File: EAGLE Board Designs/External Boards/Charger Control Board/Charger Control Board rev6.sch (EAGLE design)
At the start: 112 parts, among them U1 CPC1002N, U2 CDSOT23-T24CAN-Q

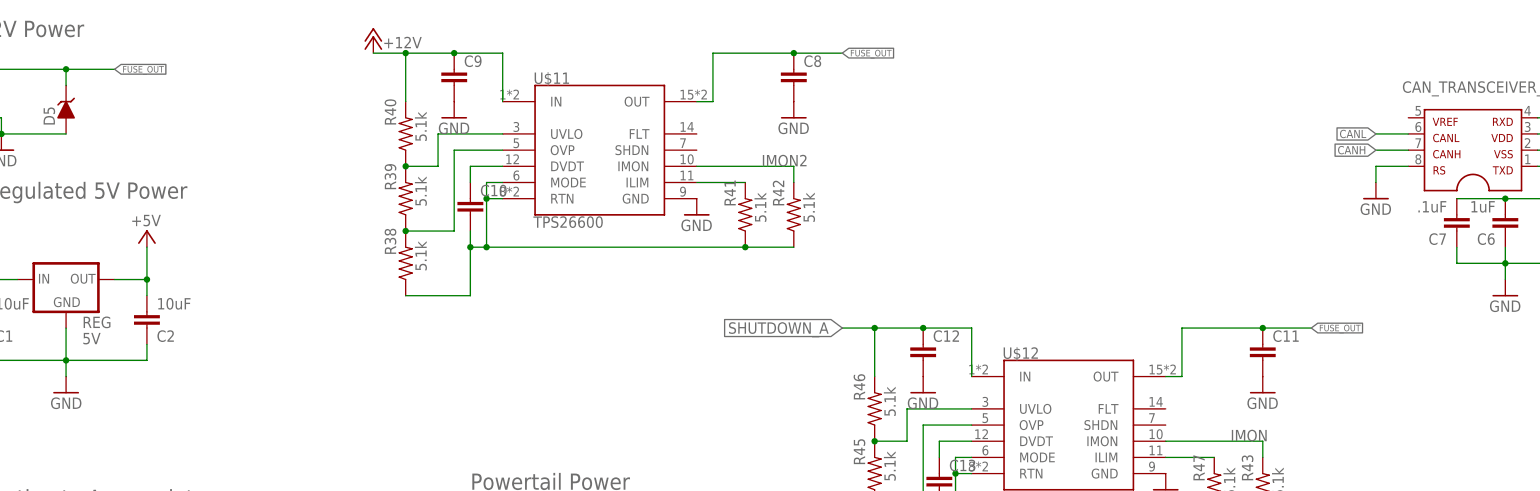
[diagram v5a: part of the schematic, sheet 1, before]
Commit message: Altered the orientation of the e-fuse and made changes to the trace widths
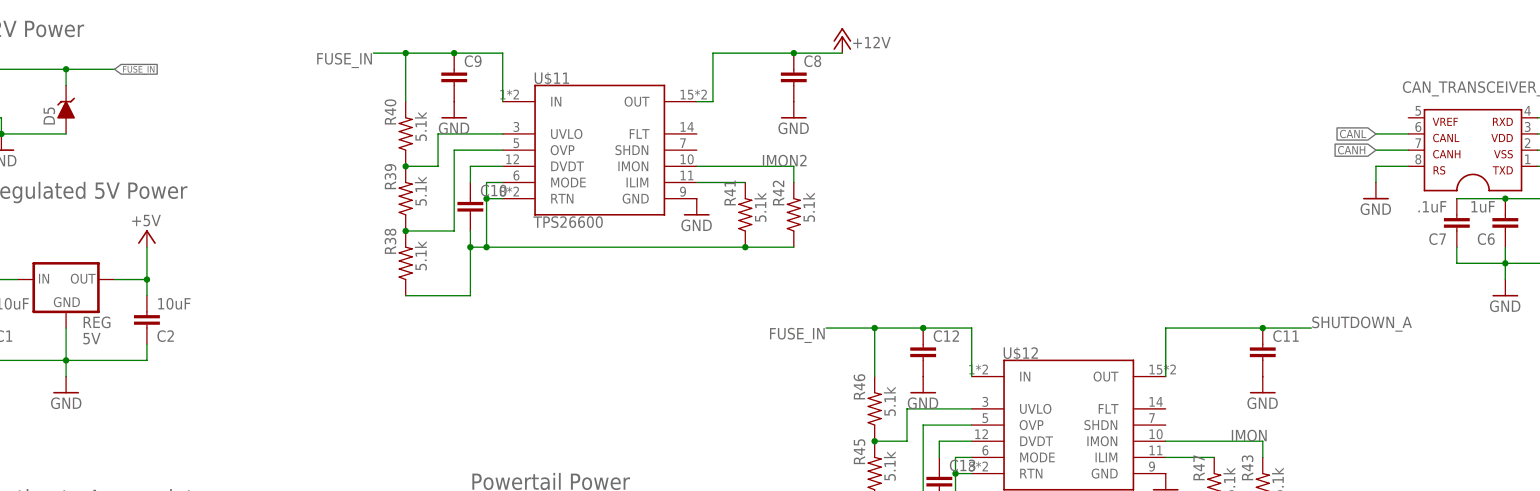
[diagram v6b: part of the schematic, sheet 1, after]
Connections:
- removed net FUSE_OUT: C11.1, C8.1, D5.C, POWER-1.S, POWER-3.S, U$11.OUT, U$12.OUT
- new net FUSE_IN: C12.1, C9.1, D5.C, POWER-1.S, POWER-3.S, R40.2, R46.2, U$11.IN, U$12.IN
- net +12V: now also C8.1, U$11.OUT; no longer C9.1, R40.2, U$11.IN
- net SHUTDOWN_A: now also C11.1, U$12.OUT; no longer C12.1, R46.2, U$12.IN
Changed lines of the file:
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@@
 <part name="R17" library="HyTechDevices" deviceset="RESISTOR" device="0603-RES" value="1k"/>
 <part name="U$7" library="HyTechFrames" deviceset="FRAME_B_L" device=""/>
-<part name="P+5" library="supply1" deviceset="+12V" device=""/>
 <part name="GND2" library="supply1" deviceset="GND" device=""/>
 <part name="REG" library="HyTechDevices" deviceset="OKI-78SR-5" device="" value="5V"/>
@@
 <attribute name="TOLERANCE" value="1%"/>
 </part>
+<part name="P+5" library="supply1" deviceset="+12V" device=""/>
 </parts>
 <sheets>
@@
 <attribute name="DRAWING_NAME" x="356.87" y="22.86" size="2.54" layer="97"/>
 </instance>
-<instance part="P+5" gate="1" x="109.22" y="254" smashed="yes">
-<attribute name="VALUE" x="116.84" y="254" size="1.778" layer="96" rot="R180"/>
-</instance>
 <instance part="GND2" gate="1" x="50.8" y="236.22" smashed="yes">
 <attribute name="VALUE" x="48.26" y="233.68" size="1.778" layer="96"/>
@@
 <attribute name="VALUE" x="252.222" y="181.61" size="1.778" layer="96" rot="R90"/>
 <attribute name="TOLERANCE" x="248.92" y="182.88" size="0.127" layer="96" rot="R90" display="off"/>
+</instance>
+<instance part="P+5" gate="1" x="182.88" y="254" smashed="yes">
+<attribute name="VALUE" x="190.5" y="254" size="1.778" layer="96" rot="R180"/>
 </instance>
 </instances>
@@
 </segment>
 <segment>
-<pinref part="U$11" gate="G$1" pin="IN"/>
-<wire x1="129.54" y1="243.84" x2="129.54" y2="251.46" width="0.1524" layer="91"/>
-<wire x1="129.54" y1="251.46" x2="121.92" y2="251.46" width="0.1524" layer="91"/>
-<pinref part="R40" gate="G$1" pin="2"/>
-<wire x1="121.92" y1="251.46" x2="114.3" y2="251.46" width="0.1524" layer="91"/>
-<wire x1="114.3" y1="251.46" x2="114.3" y2="243.84" width="0.1524" layer="91"/>
-<pinref part="C9" gate="G$1" pin="1"/>
-<junction x="121.92" y="251.46"/>
-<wire x1="114.3" y1="251.46" x2="109.22" y2="251.46" width="0.1524" layer="91"/>
-<junction x="114.3" y="251.46"/>
+<pinref part="U$11" gate="G$1" pin="OUT"/>
+<wire x1="160.02" y1="243.84" x2="162.56" y2="243.84" width="0.1524" layer="91"/>
+<wire x1="162.56" y1="243.84" x2="162.56" y2="251.46" width="0.1524" layer="91"/>
+<wire x1="162.56" y1="251.46" x2="175.26" y2="251.46" width="0.1524" layer="91"/>
+<pinref part="C8" gate="G$1" pin="1"/>
+<wire x1="175.26" y1="251.46" x2="182.88" y2="251.46" width="0.1524" layer="91"/>
+<junction x="175.26" y="251.46"/>
 <pinref part="P+5" gate="1" pin="+12V"/>
 </segment>
@@
 <net name="SHUTDOWN_A" class="0">
 <segment>
-<pinref part="U$12" gate="G$1" pin="IN"/>
-<wire x1="203.2" y1="200.66" x2="203.2" y2="208.28" width="0.1524" layer="91"/>
-<wire x1="203.2" y1="208.28" x2="195.58" y2="208.28" width="0.1524" layer="91"/>
-<pinref part="R46" gate="G$1" pin="2"/>
-<wire x1="195.58" y1="208.28" x2="187.96" y2="208.28" width="0.1524" layer="91"/>
-<wire x1="187.96" y1="208.28" x2="187.96" y2="200.66" width="0.1524" layer="91"/>
-<pinref part="C12" gate="G$1" pin="1"/>
-<junction x="195.58" y="208.28"/>
-<wire x1="187.96" y1="208.28" x2="182.88" y2="208.28" width="0.1524" layer="91"/>
-<junction x="187.96" y="208.28"/>
-<label x="182.88" y="208.28" size="1.778" layer="95" font="vector" rot="R180" xref="yes"/>
-</segment>
-</net>
-<net name="FUSE_OUT" class="0">
+<pinref part="U$12" gate="G$1" pin="OUT"/>
+<pinref part="C11" gate="G$1" pin="1"/>
+<wire x1="233.68" y1="200.66" x2="233.68" y2="208.28" width="0.1524" layer="91"/>
+<wire x1="233.68" y1="208.28" x2="248.92" y2="208.28" width="0.1524" layer="91"/>
+<wire x1="248.92" y1="208.28" x2="256.54" y2="208.28" width="0.1524" layer="91"/>
+<junction x="248.92" y="208.28"/>
+<label x="256.54" y="208.28" size="1.778" layer="95"/>
+</segment>
+</net>
+<net name="IMON" class="0">
+<segment>
+<pinref part="U$12" gate="G$1" pin="IMON"/>
+<label x="243.84" y="190.5" size="1.778" layer="95"/>
+<pinref part="R43" gate="G$1" pin="2"/>
+<wire x1="233.68" y1="190.5" x2="248.92" y2="190.5" width="0.1524" layer="91"/>
+<wire x1="248.92" y1="190.5" x2="248.92" y2="187.96" width="0.1524" layer="91"/>
+</segment>
+<segment>
+<pinref part="U$4" gate="G$1" pin="A6"/>
+<wire x1="121.92" y1="58.42" x2="124.46" y2="58.42" width="0.1524" layer="91"/>
+<label x="124.46" y="58.42" size="1.778" layer="95"/>
+</segment>
+</net>
+<net name="IMON2" class="0">
+<segment>
+<pinref part="U$11" gate="G$1" pin="IMON"/>
+<label x="170.18" y="233.68" size="1.778" layer="95"/>
+<wire x1="160.02" y1="233.68" x2="175.26" y2="233.68" width="0.1524" layer="91"/>
+<pinref part="R42" gate="G$1" pin="2"/>
+<wire x1="175.26" y1="233.68" x2="175.26" y2="231.14" width="0.1524" layer="91"/>
+</segment>
+<segment>
+<pinref part="U$4" gate="G$1" pin="A5"/>
+<wire x1="121.92" y1="55.88" x2="124.46" y2="55.88" width="0.1524" layer="91"/>
+<label x="124.46" y="55.88" size="1.778" layer="95"/>
+</segment>
+</net>
+<net name="FUSE_IN" class="0">
 <segment>
 <wire x1="68.58" y1="248.92" x2="60.96" y2="248.92" width="0.1524" layer="91"/>
@@
 </segment>
 <segment>
-<pinref part="U$11" gate="G$1" pin="OUT"/>
-<wire x1="160.02" y1="243.84" x2="162.56" y2="243.84" width="0.1524" layer="91"/>
-<wire x1="162.56" y1="243.84" x2="162.56" y2="251.46" width="0.1524" layer="91"/>
-<wire x1="162.56" y1="251.46" x2="175.26" y2="251.46" width="0.1524" layer="91"/>
-<pinref part="C8" gate="G$1" pin="1"/>
-<wire x1="175.26" y1="251.46" x2="182.88" y2="251.46" width="0.1524" layer="91"/>
-<junction x="175.26" y="251.46"/>
-<label x="182.88" y="251.46" size="1.016" layer="95" font="vector" xref="yes"/>
-</segment>
-<segment>
-<pinref part="U$12" gate="G$1" pin="OUT"/>
-<wire x1="233.68" y1="200.66" x2="236.22" y2="200.66" width="0.1524" layer="91"/>
-<wire x1="236.22" y1="200.66" x2="236.22" y2="208.28" width="0.1524" layer="91"/>
-<wire x1="236.22" y1="208.28" x2="248.92" y2="208.28" width="0.1524" layer="91"/>
-<pinref part="C11" gate="G$1" pin="1"/>
-<wire x1="248.92" y1="208.28" x2="256.54" y2="208.28" width="0.1524" layer="91"/>
-<junction x="248.92" y="208.28"/>
-<label x="256.54" y="208.28" size="1.016" layer="95" font="vector" xref="yes"/>
-</segment>
-</net>
-<net name="IMON" class="0">
-<segment>
-<pinref part="U$12" gate="G$1" pin="IMON"/>
-<label x="243.84" y="190.5" size="1.778" layer="95"/>
-<pinref part="R43" gate="G$1" pin="2"/>
-<wire x1="233.68" y1="190.5" x2="248.92" y2="190.5" width="0.1524" layer="91"/>
-<wire x1="248.92" y1="190.5" x2="248.92" y2="187.96" width="0.1524" layer="91"/>
-</segment>
-<segment>
-<pinref part="U$4" gate="G$1" pin="A6"/>
-<wire x1="121.92" y1="58.42" x2="124.46" y2="58.42" width="0.1524" layer="91"/>
-<label x="124.46" y="58.42" size="1.778" layer="95"/>
-</segment>
-</net>
-<net name="IMON2" class="0">
-<segment>
-<pinref part="U$11" gate="G$1" pin="IMON"/>
-<label x="170.18" y="233.68" size="1.778" layer="95"/>
-<wire x1="160.02" y1="233.68" x2="175.26" y2="233.68" width="0.1524" layer="91"/>
-<pinref part="R42" gate="G$1" pin="2"/>
-<wire x1="175.26" y1="233.68" x2="175.26" y2="231.14" width="0.1524" layer="91"/>
-</segment>
-<segment>
-<pinref part="U$4" gate="G$1" pin="A5"/>
-<wire x1="121.92" y1="55.88" x2="124.46" y2="55.88" width="0.1524" layer="91"/>
-<label x="124.46" y="55.88" size="1.778" layer="95"/>
-</segment>
-</net>
+<pinref part="U$11" gate="G$1" pin="IN"/>
+<wire x1="129.54" y1="243.84" x2="129.54" y2="251.46" width="0.1524" layer="91"/>
+<wire x1="129.54" y1="251.46" x2="121.92" y2="251.46" width="0.1524" layer="91"/>
+<pinref part="R40" gate="G$1" pin="2"/>
+<wire x1="121.92" y1="251.46" x2="114.3" y2="251.46" width="0.1524" layer="91"/>
+<wire x1="114.3" y1="251.46" x2="114.3" y2="243.84" width="0.1524" layer="91"/>
+<pinref part="C9" gate="G$1" pin="1"/>
+<junction x="121.92" y="251.46"/>
+<wire x1="114.3" y1="251.46" x2="109.22" y2="251.46" width="0.1524" layer="91"/>
+<junction x="114.3" y="251.46"/>
+<label x="109.22" y="251.46" size="1.778" layer="95" rot="R180"/>
+</segment>
+<segment>
+<pinref part="U$12" gate="G$1" pin="IN"/>
+<pinref part="C12" gate="G$1" pin="1"/>
+<wire x1="203.2" y1="200.66" x2="203.2" y2="208.28" width="0.1524" layer="91"/>
+<wire x1="203.2" y1="208.28" x2="195.58" y2="208.28" width="0.1524" layer="91"/>
+<pinref part="R46" gate="G$1" pin="2"/>
+<wire x1="195.58" y1="208.28" x2="187.96" y2="208.28" width="0.1524" layer="91"/>
+<wire x1="187.96" y1="208.28" x2="187.96" y2="200.66" width="0.1524" layer="91"/>
+<junction x="195.58" y="208.28"/>
+<wire x1="187.96" y1="208.28" x2="180.34" y2="208.28" width="0.1524" layer="91"/>
+<junction x="187.96" y="208.28"/>
+<label x="180.34" y="208.28" size="1.778" layer="95" rot="R180"/>
+</segment>
+</net>

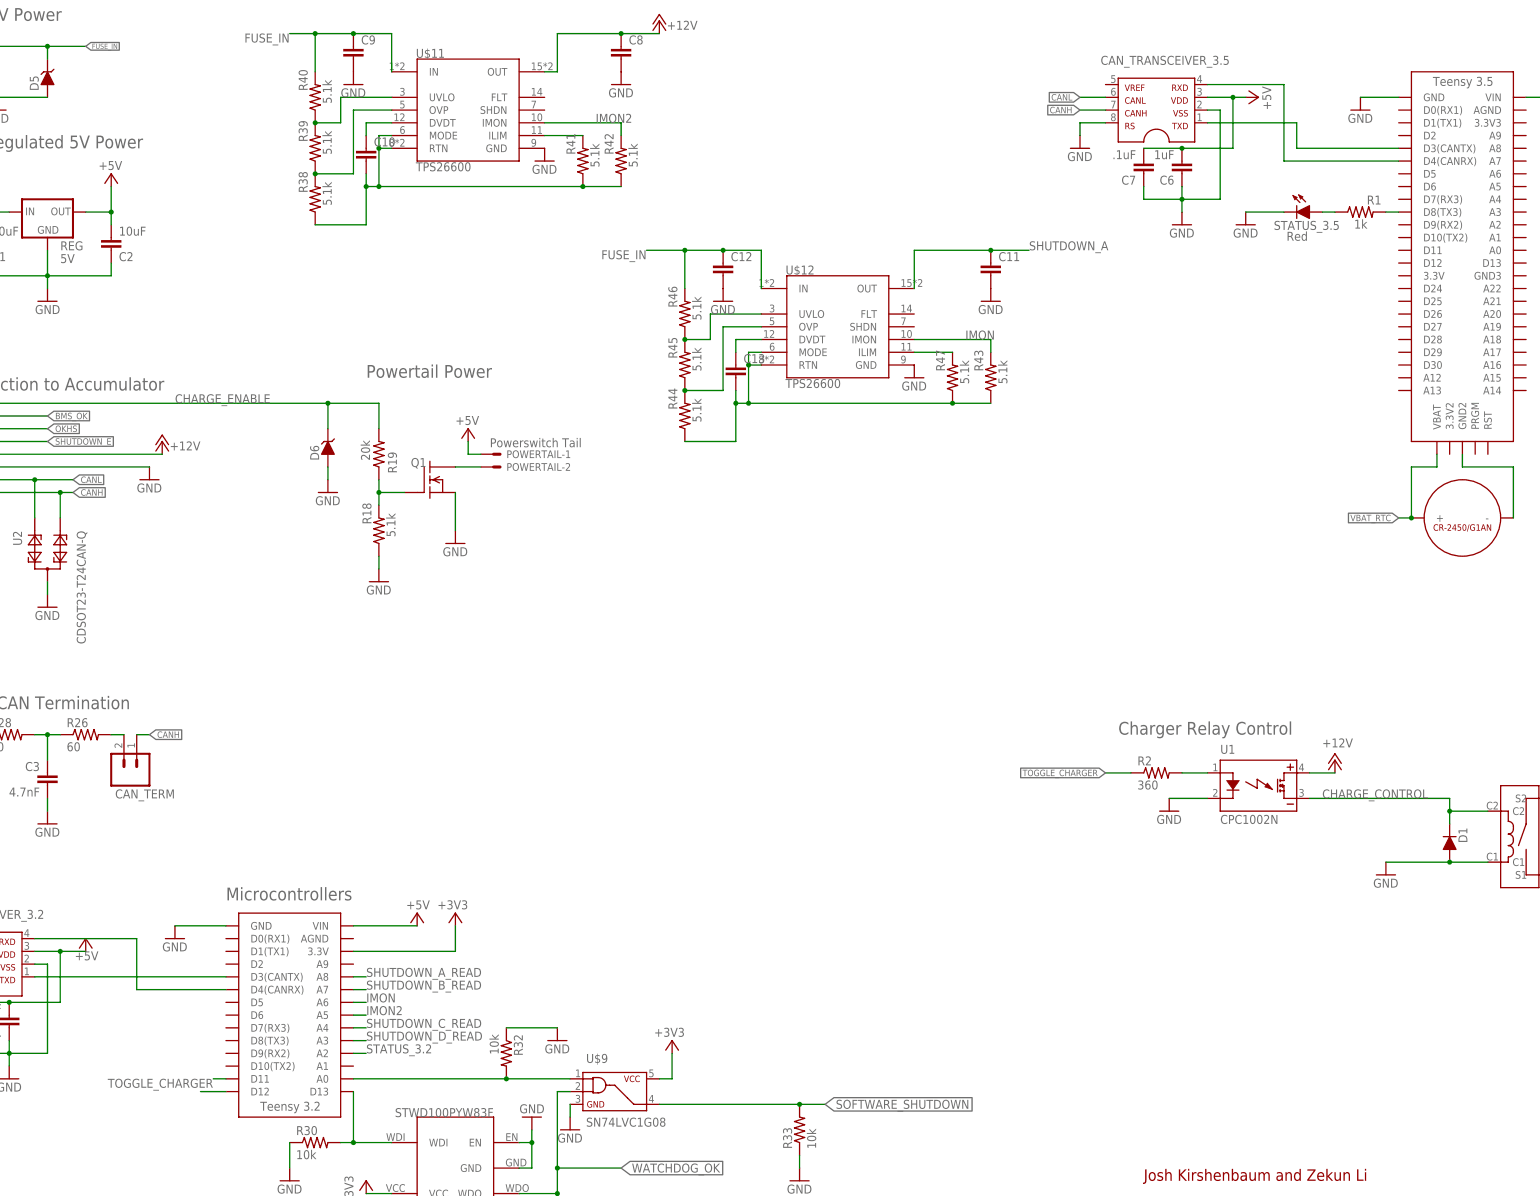
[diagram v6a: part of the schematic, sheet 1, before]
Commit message: Added resistor diode pairs for signals being monitored and added a button to reset the efuses if tripped
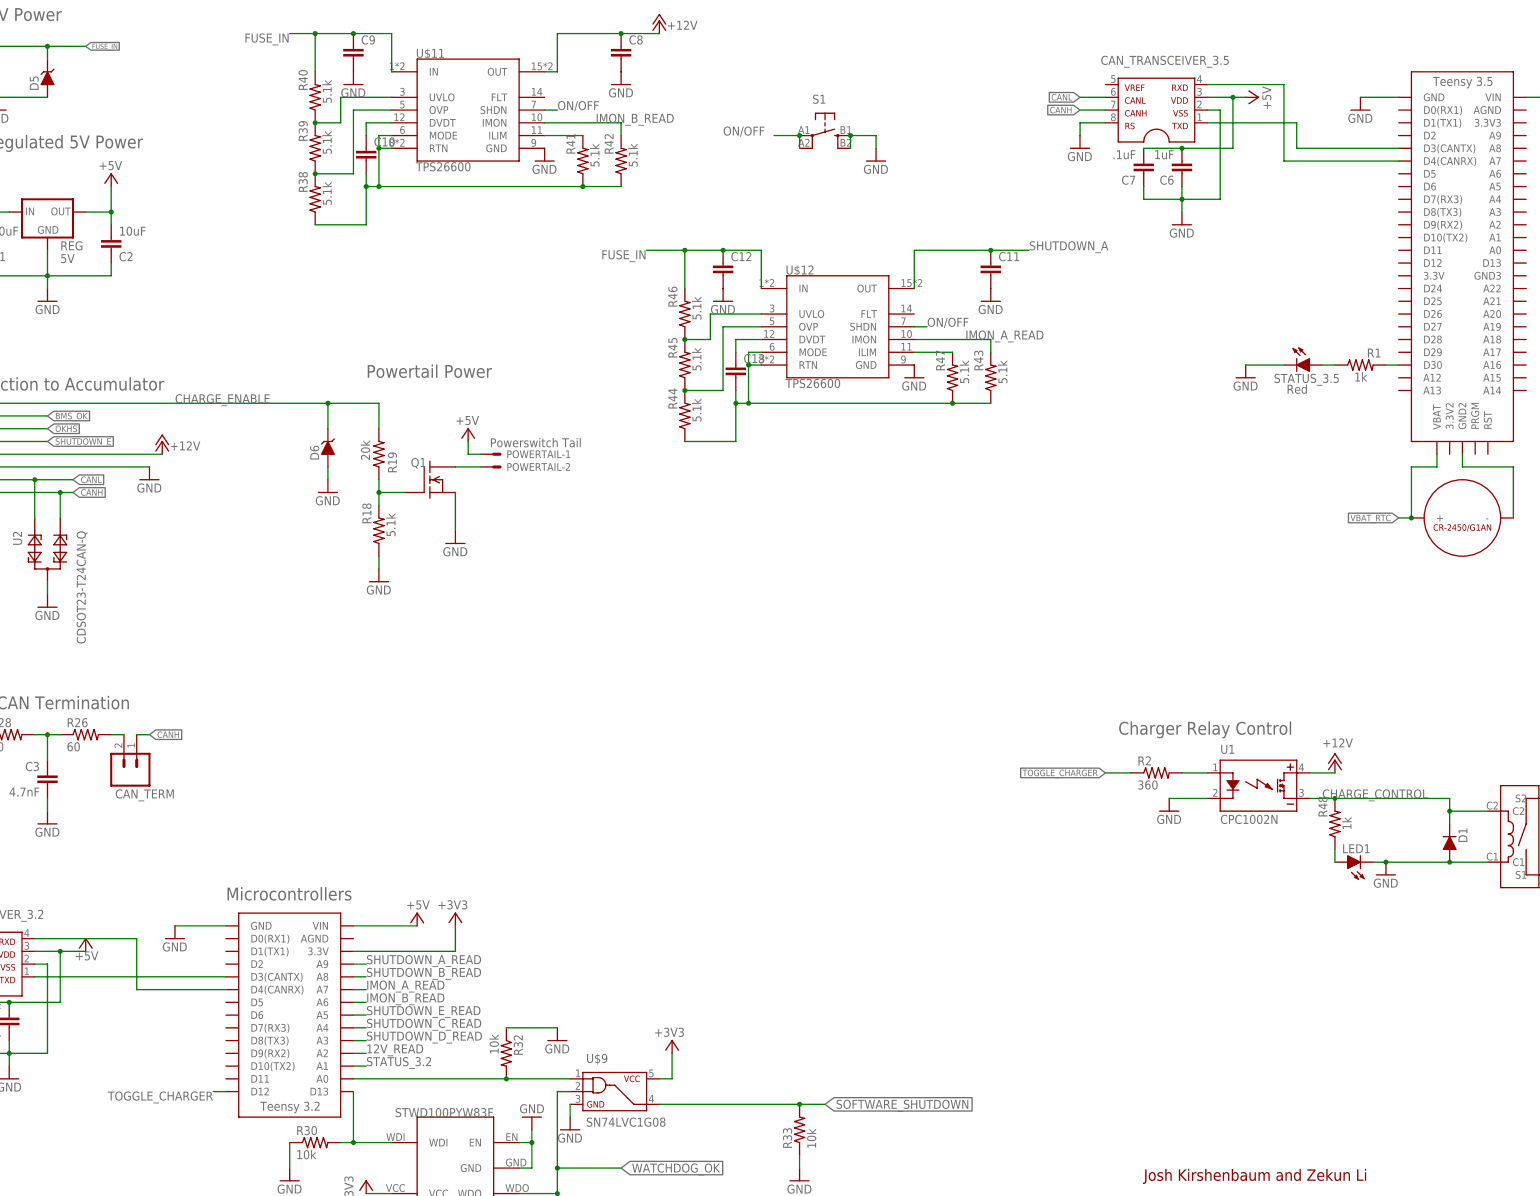
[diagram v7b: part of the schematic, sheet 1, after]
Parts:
- added D10, D15: TS4148 RYG, HyTechDevices:DIODE0805
- added LED1: (no value), HyTechDevices:LED-0603
- added R48: 1k, HyTechDevices:RESISTOR0603-RES
- added R49, R51: 43k, HyTechDevices:RESISTOR0603-RES
- added R50, R52: 12k, HyTechDevices:RESISTOR0603-RES
- added S1: (no value), HyTechDevices:BTN_10-XXSMD
- 12V_OK, BMS_OK, LATCH, OKHS, POWER_5V, SHUTDOWN_B, SHUTDOWN_C, SHUTDOWN_D, SHUTDOWN_E, SOFTWARE, STATUS_3.2, STATUS_3.5, WATCHDOG_OK: device HyTechDevices:LED-0805 -> HyTechDevices:LED-0603
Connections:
- removed net IMON: R43.2, U$12.IMON, U$4.A6
- removed net IMON2: R42.2, U$11.IMON, U$4.A5
- new net 12V_READ: R49.2, R50.1, U$4.A2
- new net IMON_A_READ: R43.2, U$12.IMON, U$4.A7
- new net IMON_B_READ: R42.2, U$11.IMON, U$4.A6
- new net N$40: LED1.A, R48.1
- new net N$42: D10.C, R49.1
- new net ON/OFF: S1.P, S1.P1, U$11.SHDN, U$12.SHDN
- new net SHUTDOWN_E_READ: R51.2, R52.1, U$4.A5
- net +12V: now also D10.A
- net CHARGE_CONTROL: now also R48.2
- net GND: now also LED1.C, R50.2, R52.2, S1.S, S1.S1
- net N$28: now also D15.C, R51.1; no longer U$4.D12
- net N$9: now also U$3.D30; no longer U$3.D8(TX3)
- net SHUTDOWN_A_READ: now also U$4.A9; no longer U$4.A8
- net SHUTDOWN_B_READ: now also U$4.A8; no longer U$4.A7
- net SHUTDOWN_E: now also D15.A
- net STATUS_3.2: now also U$4.A1; no longer U$4.A2
- net TOGGLE_CHARGER: now also U$4.D12; no longer U$4.D11
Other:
- moved on the sheet: R1, STATUS_3.5
